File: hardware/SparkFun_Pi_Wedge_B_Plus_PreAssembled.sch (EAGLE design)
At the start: 15 parts

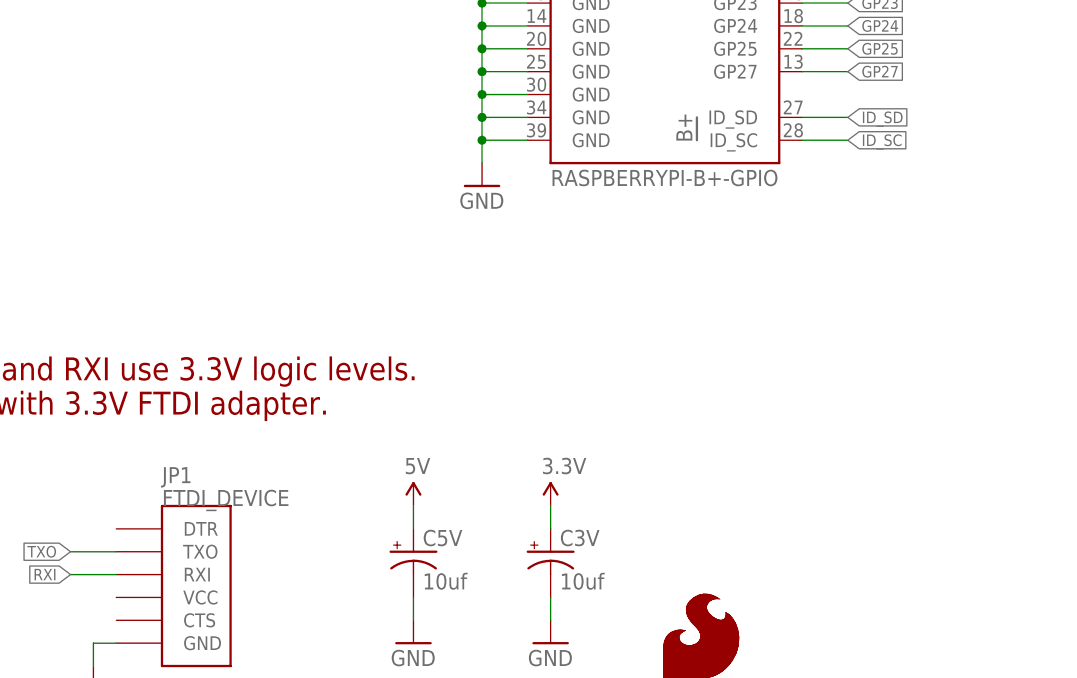
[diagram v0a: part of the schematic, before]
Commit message: Parts swapped, & old traces ripped up.
Ready for routing through the narrow neck.
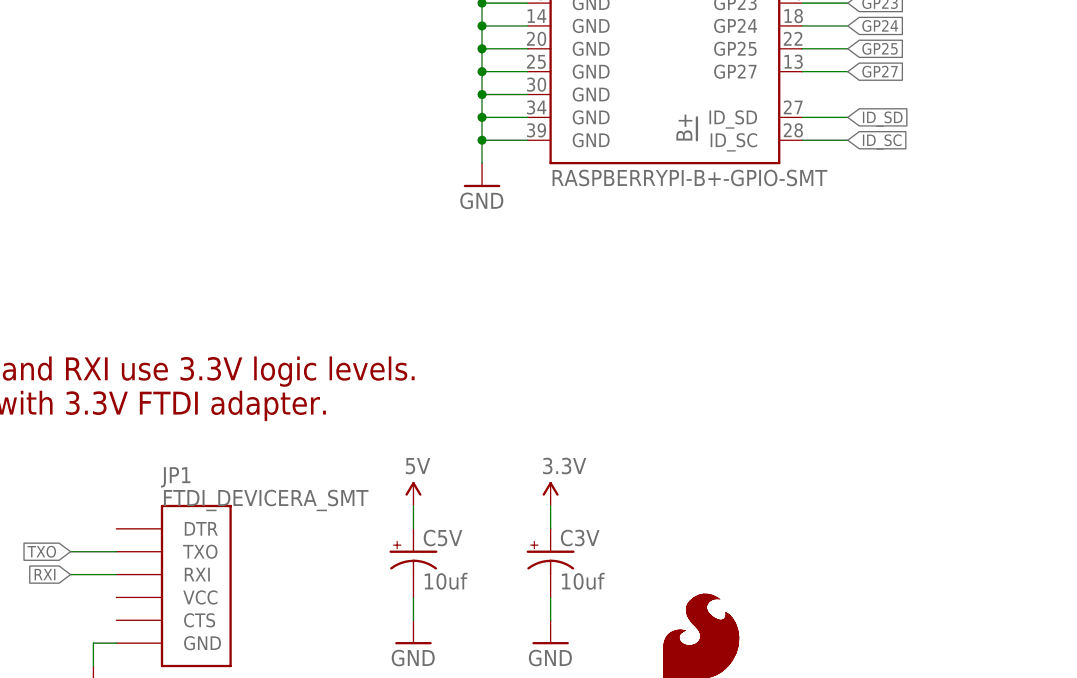
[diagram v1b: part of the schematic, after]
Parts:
- C3V, C5V: device SparkFun-Capacitors:10UF-25V-20%(PTH)KIT -> SparkFun-Capacitors:47UF-50V-20%(ELECT)
- JP1: value FTDI_DEVICE -> FTDI_DEVICERA_SMT; device SparkFun-Connectors:FTDI_DEVICE -> SparkFun-Connectors:FTDI_DEVICERA_SMT
- JP2: value RASPBERRYPI-B+-GPIO -> RASPBERRYPI-B+-GPIO-SMT; device SparkFun-Boards:RASPBERRYPI-B+-GPIO -> SparkFun-Boards:RASPBERRYPI-B+-GPIO-SMT
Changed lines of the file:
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@@
 <?xml version="1.0" encoding="utf-8"?>
 <!DOCTYPE eagle SYSTEM "eagle.dtd">
-<eagle version="6.5.0">
+<eagle version="7.3.0">
 <drawing>
 <settings>
@@
 <layer number="56" name="wert" color="7" fill="1" visible="no" active="no"/>
 <layer number="57" name="tCAD" color="7" fill="1" visible="no" active="no"/>
+<layer number="59" name="tCarbon" color="7" fill="1" visible="no" active="no"/>
+<layer number="60" name="bCarbon" color="7" fill="1" visible="no" active="no"/>
+<layer number="90" name="Modules" color="5" fill="1" visible="yes" active="yes"/>
 <layer number="91" name="Nets" color="2" fill="1" visible="yes" active="yes"/>
 <layer number="92" name="Busses" color="1" fill="1" visible="yes" active="yes"/>
@@
 <layer number="112" name="tSilk" color="7" fill="1" visible="yes" active="yes"/>
 <layer number="113" name="IDFDebug" color="4" fill="1" visible="yes" active="yes"/>
+<layer number="114" name="Badge_Outline" color="11" fill="1" visible="no" active="no"/>
 <layer number="116" name="Patch_BOT" color="9" fill="4" visible="no" active="yes"/>
+<layer number="118" name="Rect_Pads" color="7" fill="1" visible="yes" active="yes"/>
 <layer number="121" name="_tsilk" color="7" fill="1" visible="no" active="yes"/>
 <layer number="122" name="_bsilk" color="7" fill="1" visible="no" active="yes"/>
@@
 <layer number="127" name="_tValues" color="7" fill="1" visible="yes" active="yes"/>
 <layer number="128" name="_bValues" color="7" fill="1" visible="yes" active="yes"/>
+<layer number="129" name="Mask" color="7" fill="1" visible="yes" active="yes"/>
 <layer number="131" name="tAdjust" color="7" fill="1" visible="yes" active="yes"/>
 <layer number="132" name="bAdjust" color="7" fill="1" visible="yes" active="yes"/>
@@
 <layer number="223" name="223bmp" color="24" fill="1" visible="no" active="no"/>
 <layer number="224" name="224bmp" color="25" fill="1" visible="no" active="no"/>
+<layer number="225" name="225bmp" color="7" fill="1" visible="yes" active="yes"/>
+<layer number="226" name="226bmp" color="7" fill="1" visible="yes" active="yes"/>
+<layer number="227" name="227bmp" color="7" fill="1" visible="yes" active="yes"/>
+<layer number="228" name="228bmp" color="7" fill="1" visible="yes" active="yes"/>
+<layer number="229" name="229bmp" color="7" fill="1" visible="yes" active="yes"/>
+<layer number="230" name="230bmp" color="7" fill="1" visible="yes" active="yes"/>
+<layer number="231" name="231bmp" color="7" fill="1" visible="yes" active="yes"/>
 <layer number="248" name="Housing" color="7" fill="1" visible="yes" active="yes"/>
 <layer number="249" name="Edge" color="7" fill="1" visible="yes" active="yes"/>
@@
 <layer number="251" name="SMDround" color="12" fill="11" visible="no" active="no"/>
 <layer number="254" name="cooling" color="7" fill="1" visible="no" active="yes"/>
+<layer number="255" name="routoute" color="7" fill="1" visible="yes" active="yes"/>
 </layers>
 <schematic xreflabel="%F%N/%S.%C%R" xrefpart="/%S.%C%R">
@@
 </classes>
 <parts>
-<part name="JP1" library="SparkFun-Connectors" deviceset="FTDI_DEVICE" device=""/>
+<part name="JP1" library="SparkFun-Connectors" deviceset="FTDI_DEVICE" device="RA_SMT" value="FTDI_DEVICERA_SMT"/>
 <part name="FRAME2" library="SparkFun-Aesthetics" deviceset="FRAME-LETTER" device=""/>
 <part name="GND1" library="SparkFun" deviceset="GND" device=""/>
@@
 <part name="STANDOFF1" library="SparkFun-Electromechanical" deviceset="STAND-OFF" device=""/>
 <part name="STANDOFF2" library="SparkFun-Electromechanical" deviceset="STAND-OFF" device=""/>
-<part name="C5V" library="SparkFun-Capacitors" deviceset="10UF-25V-20%(PTH)" device="KIT" value="10uf"/>
-<part name="C3V" library="SparkFun-Capacitors" deviceset="10UF-25V-20%(PTH)" device="KIT" value="10uf"/>
+<part name="C5V" library="SparkFun-Capacitors" deviceset="47UF-50V-20%(ELECT)" device="" value="10uf"/>
+<part name="C3V" library="SparkFun-Capacitors" deviceset="47UF-50V-20%(ELECT)" device="" value="10uf"/>
 <part name="GND4" library="SparkFun" deviceset="GND" device=""/>
 <part name="GND8" library="SparkFun" deviceset="GND" device=""/>
@@
 <part name="SUPPLY10" library="SparkFun-Aesthetics" deviceset="3.3V" device=""/>
 <part name="U$2" library="SparkFun-Aesthetics" deviceset="BREADBOARD_PATTERN" device=""/>
-<part name="JP2" library="SparkFun-Boards" deviceset="RASPBERRYPI-B+-GPIO" device=""/>
+<part name="JP2" library="SparkFun-Boards" deviceset="RASPBERRYPI-B+-GPIO" device="-SMT" value="RASPBERRYPI-B+-GPIO-SMT"/>
 <part name="JP3" library="SparkFun-Connectors" deviceset="M17" device="KIT"/>
 <part name="JP4" library="SparkFun-Connectors" deviceset="M17" device="KIT"/>

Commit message: A few touch-ups before review.
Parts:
- LOGO1: value SFE_LOGO_NAME_FLAME.2_INCH -> SFE_LOGO_NAME.2_INCH; device SparkFun-Aesthetics:SFE_LOGO_NAME_FLAME.2_INCH -> SparkFun-Aesthetics:SFE_LOGO_NAME.2_INCH
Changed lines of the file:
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@@
 <part name="FRAME2" library="SparkFun-Aesthetics" deviceset="FRAME-LETTER" device=""/>
 <part name="GND1" library="SparkFun" deviceset="GND" device=""/>
-<part name="LOGO1" library="SparkFun-Aesthetics" deviceset="SFE_LOGO_NAME_FLAME" device=".2_INCH"/>
+<part name="LOGO1" library="SparkFun-Aesthetics" deviceset="SFE_LOGO_NAME" device=".2_INCH"/>
 <part name="STANDOFF1" library="SparkFun-Electromechanical" deviceset="STAND-OFF" device=""/>
 <part name="STANDOFF2" library="SparkFun-Electromechanical" deviceset="STAND-OFF" device=""/>
@@
 <instance part="FRAME2" gate="G$2" x="147.32" y="0"/>
 <instance part="GND1" gate="1" x="25.4" y="20.32"/>
-<instance part="LOGO1" gate="G$1" x="55.88" y="5.08"/>
+<instance part="LOGO1" gate="G$1" x="64.77" y="5.334"/>
 <instance part="STANDOFF1" gate="G$1" x="246.38" y="30.48"/>
 <instance part="STANDOFF2" gate="G$1" x="246.38" y="33.02"/>
@@
 <instance part="SUPPLY13" gate="G$1" x="71.12" y="139.7"/>
 <instance part="SUPPLY14" gate="G$1" x="60.96" y="139.7"/>
-<instance part="LOGO2" gate="G$1" x="55.88" y="5.08"/>
+<instance part="LOGO2" gate="G$1" x="66.04" y="5.08"/>
 <instance part="LOGO3" gate="G$1" x="236.22" y="38.1"/>
 <instance part="LOGO4" gate="G$1" x="236.22" y="38.1"/>

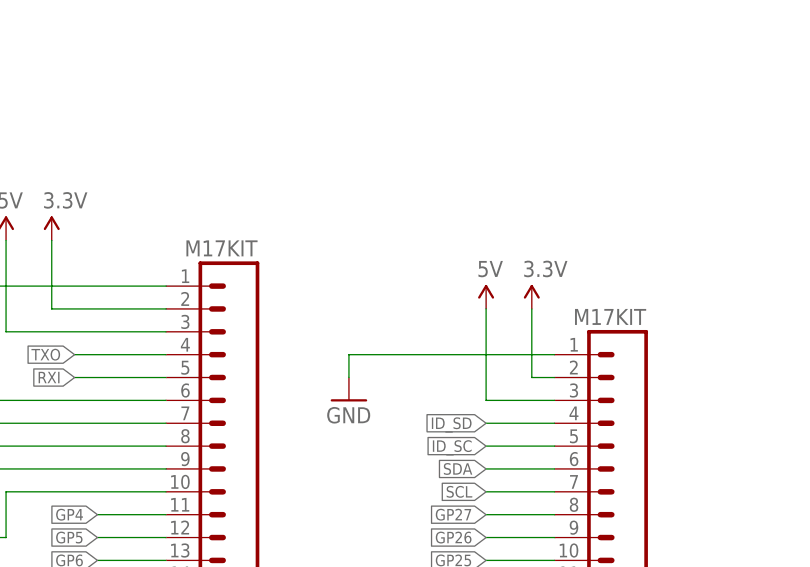
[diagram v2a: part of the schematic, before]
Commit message: Added missing PROD_IDs.
Also apparently picked up huge changes from logo revamp in aesthetics
library.  This commit is huge, but with no physical changes to board or
schematic.
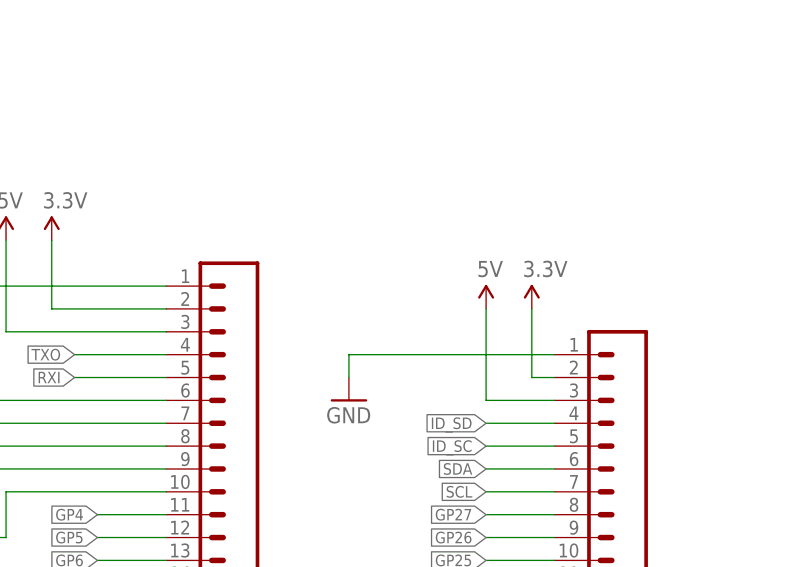
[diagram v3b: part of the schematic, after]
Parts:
- JP3, JP4: value M17KIT -> (none)
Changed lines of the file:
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@@
 <instance part="JP1" gate="G$1" x="33.02" y="33.02"/>
 <instance part="FRAME2" gate="G$1" x="0" y="0"/>
-<instance part="FRAME2" gate="G$2" x="147.32" y="0"/>
+<instance part="FRAME2" gate="V" x="147.32" y="0"/>
 <instance part="GND1" gate="1" x="25.4" y="20.32"/>
 <instance part="LOGO1" gate="G$1" x="64.77" y="5.334"/>

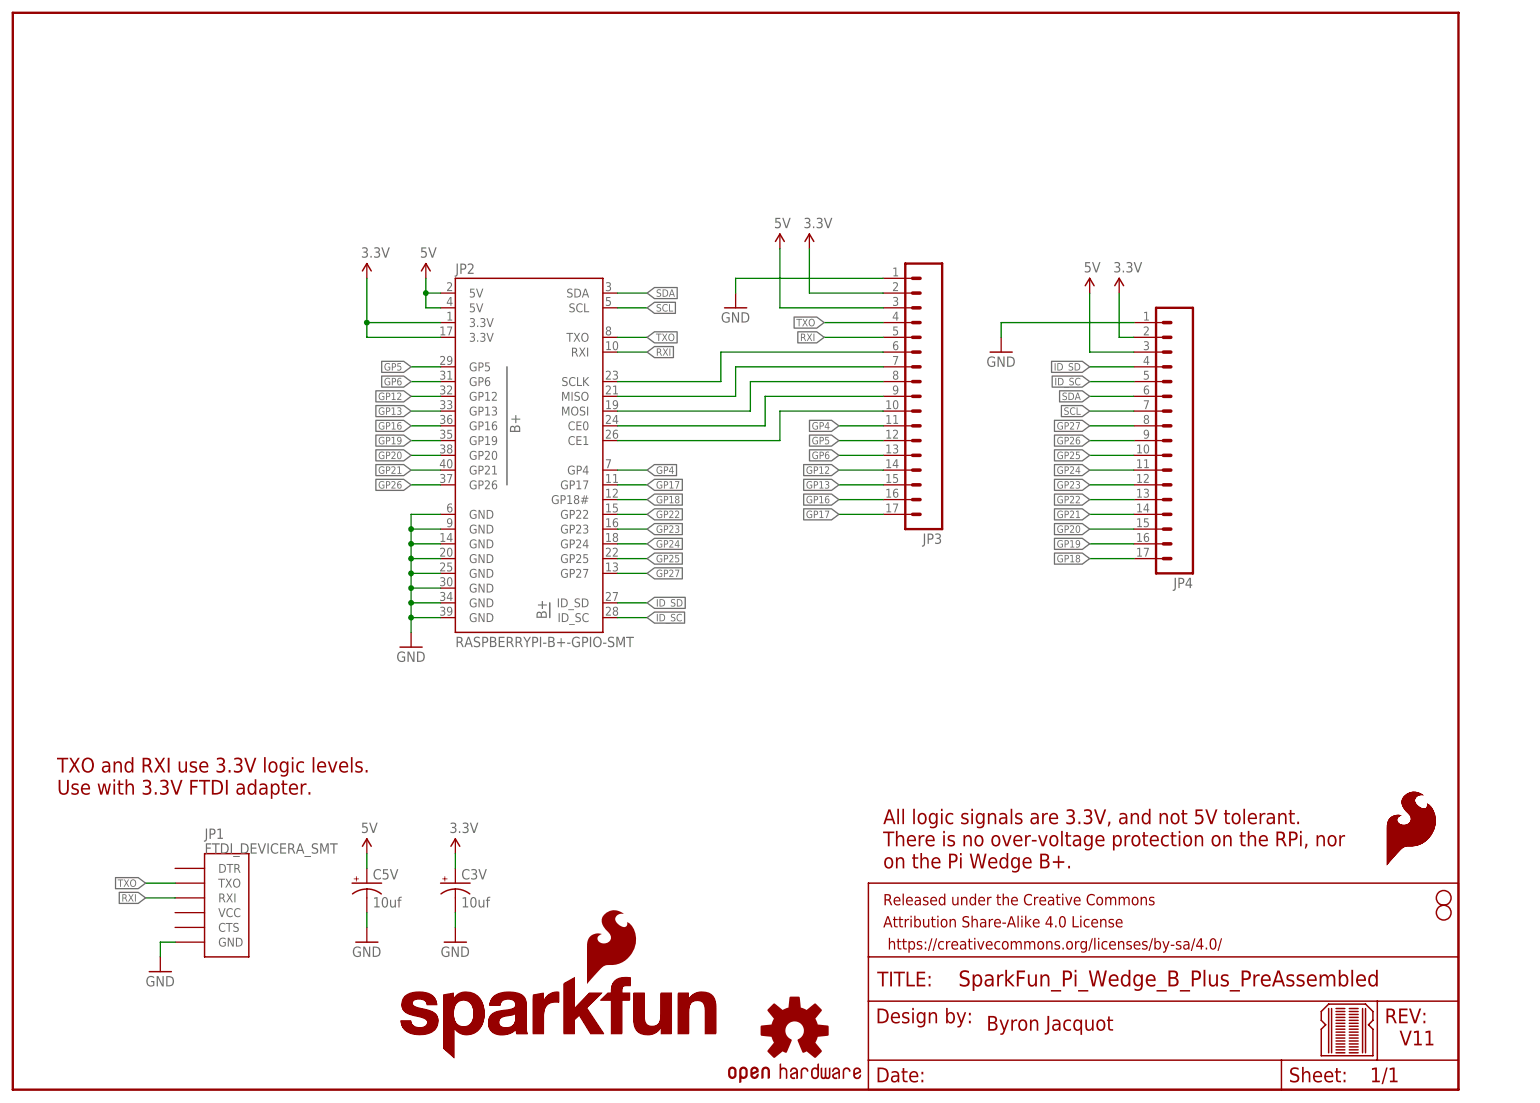
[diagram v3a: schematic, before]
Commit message: Fixing review issues.
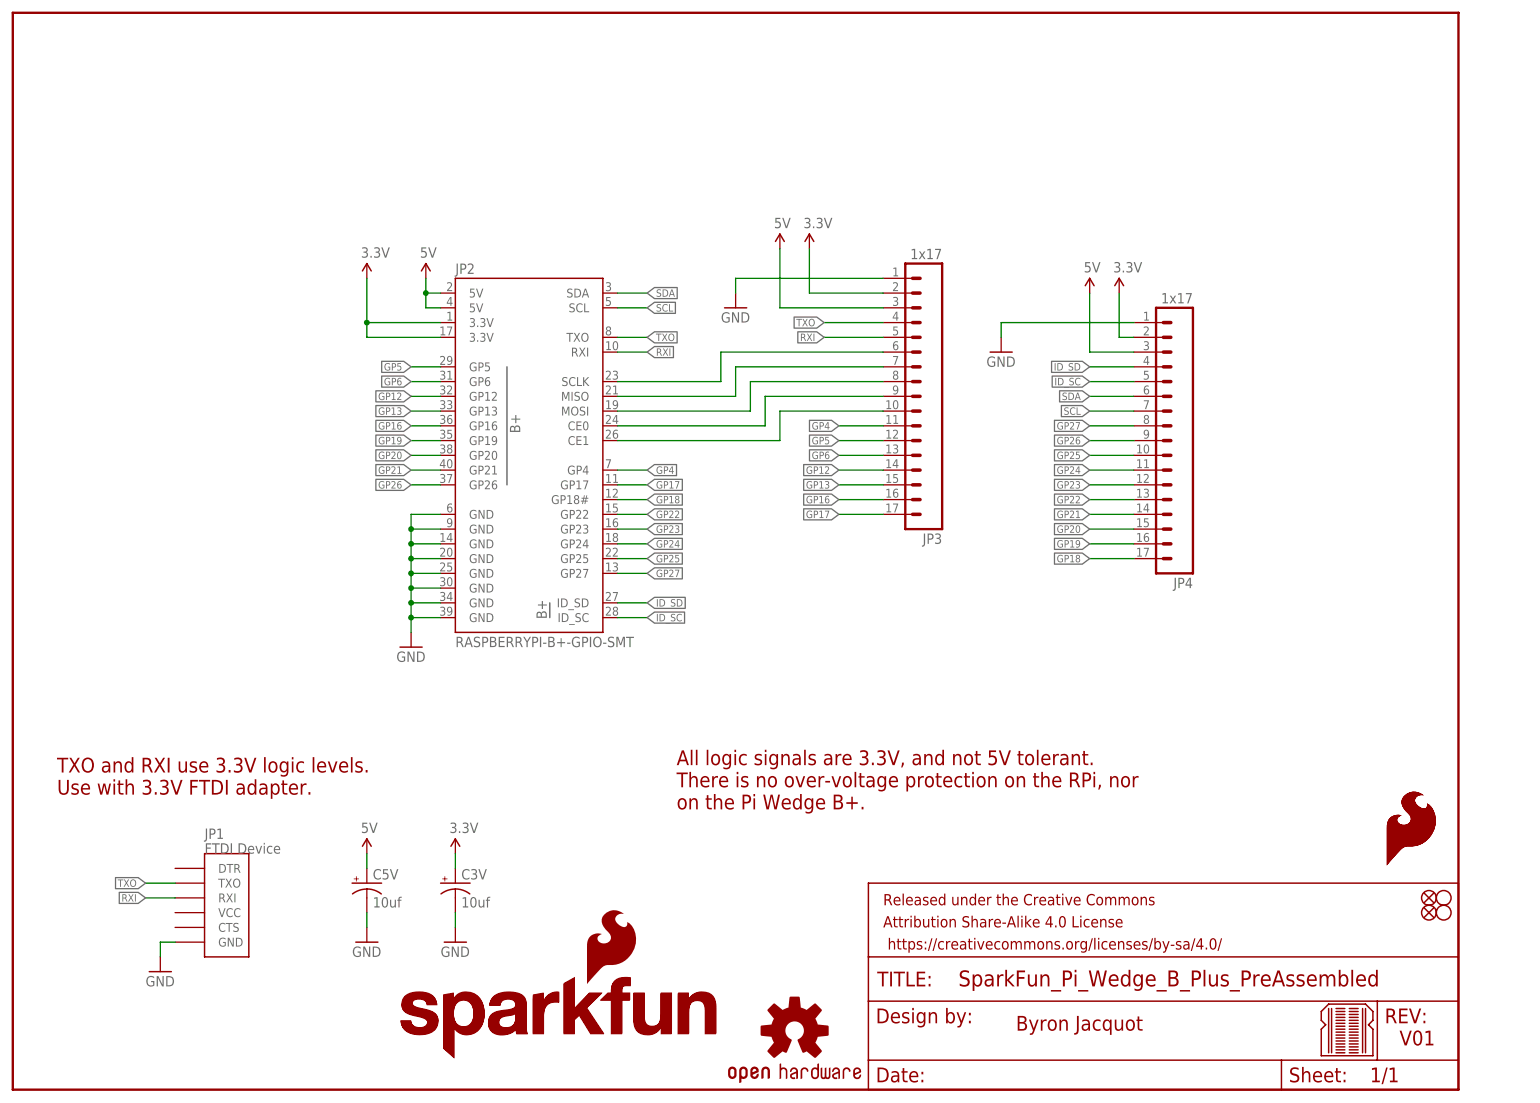
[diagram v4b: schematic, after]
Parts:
- added FID1, FID2: FIDUCIALUFIDUCIAL, SparkFun-Aesthetics:FIDUCIALUFIDUCIAL
- JP1: value FTDI_DEVICERA_SMT -> FTDI Device
- JP3, JP4: value (none) -> 1x17
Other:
- note added: "V01"
- note removed: "V11"
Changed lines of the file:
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@@
 </classes>
 <parts>
-<part name="JP1" library="SparkFun-Connectors" deviceset="FTDI_DEVICE" device="RA_SMT" value="FTDI_DEVICERA_SMT"/>
+<part name="JP1" library="SparkFun-Connectors" deviceset="FTDI_DEVICE" device="RA_SMT" value="FTDI Device"/>
 <part name="FRAME2" library="SparkFun-Aesthetics" deviceset="FRAME-LETTER" device=""/>
 <part name="GND1" library="SparkFun" deviceset="GND" device=""/>
@@
 <part name="U$2" library="SparkFun-Aesthetics" deviceset="BREADBOARD_PATTERN" device=""/>
 <part name="JP2" library="SparkFun-Boards" deviceset="RASPBERRYPI-B+-GPIO" device="-SMT" value="RASPBERRYPI-B+-GPIO-SMT"/>
-<part name="JP3" library="SparkFun-Connectors" deviceset="M17" device="KIT"/>
-<part name="JP4" library="SparkFun-Connectors" deviceset="M17" device="KIT"/>
+<part name="JP3" library="SparkFun-Connectors" deviceset="M17" device="KIT" value="1x17"/>
+<part name="JP4" library="SparkFun-Connectors" deviceset="M17" device="KIT" value="1x17"/>
 <part name="GND2" library="SparkFun" deviceset="GND" device=""/>
 <part name="SUPPLY7" library="SparkFun-Aesthetics" deviceset="3.3V" device=""/>
@@
 <part name="LOGO4" library="SparkFun-Aesthetics" deviceset="SFE_LOGO_FLAME" device=".1_INCH"/>
 <part name="LOGO5" library="SparkFun-Aesthetics" deviceset="OSHW-LOGO" device="S"/>
+<part name="FID1" library="SparkFun-Aesthetics" deviceset="FIDUCIAL" device="UFIDUCIAL"/>
+<part name="FID2" library="SparkFun-Aesthetics" deviceset="FIDUCIAL" device="UFIDUCIAL"/>
 </parts>
 <sheets>
 <sheet>
 <plain>
-<text x="167.64" y="10.16" size="2.54" layer="94">Byron Jacquot</text>
-<text x="238.76" y="7.62" size="2.54" layer="94">V11</text>
-<text x="149.86" y="38.1" size="2.54" layer="94">All logic signals are 3.3V, and not 5V tolerant.
+<text x="172.72" y="10.16" size="2.54" layer="94" font="vector">Byron Jacquot</text>
+<text x="238.76" y="7.62" size="2.54" layer="94" font="vector">V01</text>
+<text x="114.3" y="48.26" size="2.54" layer="94" font="vector">All logic signals are 3.3V, and not 5V tolerant.
 There is no over-voltage protection on the RPi, nor
 on the Pi Wedge B+.</text>
-<text x="7.62" y="50.8" size="2.54" layer="94">TXO and RXI use 3.3V logic levels.
+<text x="7.62" y="50.8" size="2.54" layer="94" font="vector">TXO and RXI use 3.3V logic levels.
 Use with 3.3V FTDI adapter.</text>
 </plain>
@@
 <instance part="LOGO4" gate="G$1" x="236.22" y="38.1"/>
 <instance part="LOGO5" gate="G$1" x="134.62" y="10.16"/>
+<instance part="FID1" gate="G$1" x="243.84" y="33.02"/>
+<instance part="FID2" gate="G$1" x="243.84" y="30.48"/>
 </instances>
 <busses>
